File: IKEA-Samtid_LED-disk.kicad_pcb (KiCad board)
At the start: 2 copper layers, 40.5 x 40.5 mm, 0 parts

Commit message: Stuff.
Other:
- board size 40.5 x 40.5 mm -> 100 x 100 mm
- board text added: "align with spoke"
- board text added: "bottom keepout"
- board text added: "top keepout"
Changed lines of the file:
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@@
-(kicad_pcb (version 3) (host pcbnew "(2014-06-29 BZR 4957)-product")
+(kicad_pcb (version 4) (host pcbnew "(2014-07-07 BZR 4985)-product")
   (general
     (links 0)
     (no_connects 0)
-    (area 117.649999 62.649999 182.350001 127.350001)
+    (area 99.899999 44.899999 204.312359 145.100001)
     (thickness 1.6002)
-    (drawings 2)
+    (drawings 13)
     (tracks 0)
     (zones 0)
@@
   )
   (layers
-    (15 Front signal)
-    (0 Back signal)
-    (18 B.Paste user)
-    (19 F.Paste user)
-    (20 B.SilkS user)
-    (21 F.SilkS user)
-    (22 B.Mask user)
-    (23 F.Mask user)
-    (26 Eco1.User user)
-    (28 Edge.Cuts user)
+    (0 Front signal)
+    (31 Back signal)
+    (34 B.Paste user)
+    (35 F.Paste user)
+    (36 B.SilkS user)
+    (37 F.SilkS user)
+    (38 B.Mask user)
+    (39 F.Mask user)
+    (42 Eco1.User user)
+    (44 Edge.Cuts user)
   )
   (setup
@@
     (visible_elements 7FFFFF7F)
     (pcbplotparams
-      (layerselection 352092161)
+      (layerselection 0x014fc_80000001)
       (usegerberextensions true)
+      (gerberprecision 5)
       (excludeedgelayer true)
-      (linewidth 0.150000)
+      (linewidth 0.200000)
       (plotframeref false)
       (viasonmask false)
@@
     (uvia_drill 0.127)
   )
-  (gr_circle (center 150 95) (end 182.25 95) (layer Eco1.User) (width 0.2))
+  (gr_arc (start 150 95) (end 123.25 106.25) (angle 99.41721335) (layer F.SilkS) (width 0.2))
+  (gr_arc (start 150 95) (end 172.75 113) (angle 104.2890517) (layer F.SilkS) (width 0.2))
+  (gr_arc (start 150 95) (end 156.75 66.75) (angle 99.18167573) (layer F.SilkS) (width 0.2))
+  (gr_circle (center 150 95) (end 200 95) (layer Edge.Cuts) (width 0.2))
+  (gr_circle (center 150 68.75) (end 152.25 68.75) (layer Edge.Cuts) (width 0.2))
+  (gr_line (start 150 73) (end 150 64.5) (angle 90) (layer F.SilkS) (width 2))
+  (gr_text "align with \n\n\nspoke" (at 149.75 68.249999 90) (layer F.SilkS)
+    (effects (font (size 1.5 1.5) (thickness 0.3)))
+  )
+  (gr_text "top keepout" (at 176.499998 94.75 90) (layer F.SilkS)
+    (effects (font (size 1 1) (thickness 0.2)))
+  )
+  (gr_text "bottom keepout" (at 180.000002 94.750002 90) (layer B.SilkS)
+    (effects (font (size 1 1) (thickness 0.2)))
+  )
+  (gr_line (start 131 106) (end 123.5 110.25) (layer F.SilkS) (width 2))
+  (gr_line (start 169 106) (end 176.5 110.25) (layer F.SilkS) (width 2))
+  (gr_circle (center 150 95) (end 182.25 95) (layer B.SilkS) (width 0.2))
   (gr_circle (center 150 95) (end 170.25 95) (layer Edge.Cuts) (width 0.2))
 )

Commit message: More stuff.
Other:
- net class Default: clearance 0.2032 -> 0.254; trace_width 0.2032 -> 0.254; via_dia 0.635 -> 0.889; via_drill 0.3302 -> 0.635
- rule trace_clearance: 0.2032 -> 0.254
- rule trace_min: 0.2032 -> 0.254
- rule via_min_drill: 0.3302 -> 0.508
- rule via_min_size: 0.635 -> 0.889
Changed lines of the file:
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@@
-(kicad_pcb (version 4) (host pcbnew "(2014-07-07 BZR 4985)-product")
+(kicad_pcb (version 3) (host pcbnew "(2014-06-29 BZR 4957)-product")
   (general
     (links 0)
     (no_connects 0)
-    (area 99.899999 44.899999 204.312359 145.100001)
-    (thickness 1.6002)
+    (area 99.899999 44.899999 200.100001 145.100001)
+    (thickness 1.6)
     (drawings 13)
     (tracks 0)
@@
   )
   (layers
-    (0 Front signal)
-    (31 Back signal)
-    (34 B.Paste user)
-    (35 F.Paste user)
-    (36 B.SilkS user)
-    (37 F.SilkS user)
-    (38 B.Mask user)
-    (39 F.Mask user)
-    (42 Eco1.User user)
-    (44 Edge.Cuts user)
+    (15 F.Cu signal)
+    (0 B.Cu signal)
+    (18 B.Paste user)
+    (19 F.Paste user)
+    (20 B.SilkS user)
+    (21 F.SilkS user)
+    (22 B.Mask user)
+    (23 F.Mask user)
+    (26 Eco1.User user)
+    (28 Edge.Cuts user)
   )
   (setup
-    (last_trace_width 0.2032)
-    (user_trace_width 0.2032)
-    (user_trace_width 0.3048)
-    (user_trace_width 0.4064)
-    (user_trace_width 0.508)
-    (user_trace_width 0.762)
-    (user_trace_width 1.016)
-    (user_trace_width 1.27)
-    (trace_clearance 0.2032)
-    (zone_clearance 0.25)
+    (last_trace_width 0.254)
+    (trace_clearance 0.254)
+    (zone_clearance 0.508)
     (zone_45_only no)
-    (trace_min 0.2032)
+    (trace_min 0.254)
     (segment_width 0.2)
     (edge_width 0.2)
-    (via_size 0.635)
-    (via_drill 0.3302)
-    (via_min_size 0.635)
-    (via_min_drill 0.3302)
+    (via_size 0.889)
+    (via_drill 0.635)
+    (via_min_size 0.889)
+    (via_min_drill 0.508)
     (uvia_size 0.508)
     (uvia_drill 0.127)
@@
     (mod_text_size 1 1)
     (mod_text_width 0.2)
-    (pad_size 1.651 1.65)
-    (pad_drill 0)
+    (pad_size 1.8 3.4)
+    (pad_drill 0.6)
     (pad_to_mask_clearance 0)
     (aux_axis_origin 0 0)
-    (visible_elements 7FFFFF7F)
+    (visible_elements FFFFFF7F)
     (pcbplotparams
-      (layerselection 0x014fc_80000001)
+      (layerselection 352092161)
       (usegerberextensions true)
-      (gerberprecision 5)
       (excludeedgelayer true)
-      (linewidth 0.200000)
+      (linewidth 0.100000)
       (plotframeref false)
       (viasonmask false)
@@
       (hpglpenspeed 20)
       (hpglpendiameter 15)
-      (hpglpenoverlay 0)
+      (hpglpenoverlay 2)
       (psnegative false)
       (psa4output false)
@@
   (net 0 "")
   (net_class Default "This is the default net class."
-    (clearance 0.2032)
-    (trace_width 0.2032)
-    (via_dia 0.635)
-    (via_drill 0.3302)
+    (clearance 0.254)
+    (trace_width 0.254)
+    (via_dia 0.889)
+    (via_drill 0.635)
     (uvia_dia 0.508)
     (uvia_drill 0.127)

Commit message: Trying to be creative.
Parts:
- added LED?: VAL**, my_parts:MADW__PLCC4-5050, F.Cu at (150.2, 54.5)
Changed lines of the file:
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@@
     (tracks 0)
     (zones 0)
-    (modules 0)
+    (modules 1)
     (nets 1)
   )
@@
     (22 B.Mask user)
     (23 F.Mask user)
+    (25 Cmts.User user)
     (26 Eco1.User user)
     (28 Edge.Cuts user)
@@
       (plotinvisibletext false)
       (padsonsilk false)
-      (subtractmaskfromsilk true)
+      (subtractmaskfromsilk false)
       (outputformat 1)
       (mirror false)
@@
     (uvia_drill 0.127)
   )
+  (module my_parts:MADW__PLCC4-5050 (layer F.Cu)
+    (at 150.25 54.5)
+    (fp_text reference LED? (at 0 -4.75) (layer F.SilkS)
+      (effects (font (size 1 1) (thickness 0.2)))
+    )
+    (fp_text value VAL** (at 0 4.85) (layer F.SilkS) hide
+      (effects (font (size 1 1) (thickness 0.2)))
+    )
+    (fp_line (start 1.65 -1) (end 1.2 -0.25) (layer F.SilkS) (width 0.2032))
+    (fp_line (start 1.2 -0.25) (end 2.1 -0.25) (layer F.SilkS) (width 0.2032))
+    (fp_line (start 2.1 -0.25) (end 1.65 -1) (layer F.SilkS) (width 0.2032))
+    (fp_line (start -2.5 -1) (end -2.5 1) (layer F.SilkS) (width 0.2032))
+    (fp_line (start -0.5 2.5) (end 0.5 2.5) (layer F.SilkS) (width 0.2032))
+    (fp_line (start 2.5 -1) (end 2.5 1) (layer F.SilkS) (width 0.2032))
+    (fp_line (start -0.5 -2.5) (end 0.5 -2.5) (layer F.SilkS) (width 0.2032))
+    (fp_line (start 2.1 2.5) (end 2.5 2.5) (layer Dwgs.User) (width 0.2032))
+    (fp_line (start -1.2 2.5) (end 1.2 2.5) (layer Dwgs.User) (width 0.2032))
+    (fp_line (start -2.5 2.5) (end -2.1 2.5) (layer Dwgs.User) (width 0.2032))
+    (fp_line (start 2.1 -2.5) (end 2.5 -2.5) (layer Dwgs.User) (width 0.2032))
+    (fp_line (start -1.2 -2.5) (end 1.2 -2.5) (layer Dwgs.User) (width 0.2032))
+    (fp_line (start -2.5 -2.5) (end -2.1 -2.5) (layer Dwgs.User) (width 0.2032))
+    (fp_line (start -2.1 -2.7) (end -1.2 -2.7) (layer Dwgs.User) (width 0.2032))
+    (fp_line (start -1.2 -2.7) (end -1.2 -1.8) (layer Dwgs.User) (width 0.2032))
+    (fp_line (start -1.2 -1.8) (end -2.1 -1.8) (layer Dwgs.User) (width 0.2032))
+    (fp_line (start -2.1 -1.8) (end -2.1 -2.7) (layer Dwgs.User) (width 0.2032))
+    (fp_line (start 2.1 -2.7) (end 1.2 -2.7) (layer Dwgs.User) (width 0.2032))
+    (fp_line (start 1.2 -2.7) (end 1.2 -1.8) (layer Dwgs.User) (width 0.2032))
+    (fp_line (start 1.2 -1.8) (end 2.1 -1.8) (layer Dwgs.User) (width 0.2032))
+    (fp_line (start 2.1 -1.8) (end 2.1 -2.7) (layer Dwgs.User) (width 0.2032))
+    (fp_line (start -3 3.85) (end -3 -3.85) (layer F.SilkS) (width 0.2))
+    (fp_line (start 3 3.85) (end -3 3.85) (layer F.SilkS) (width 0.2))
+    (fp_line (start -3 -3.85) (end 3 -3.85) (layer F.SilkS) (width 0.2))
+    (fp_line (start 3 -3.85) (end 3 3.85) (layer F.SilkS) (width 0.2))
+    (fp_line (start -2.1 2.7) (end -2.1 1.8) (layer Dwgs.User) (width 0.2))
+    (fp_line (start -2.1 1.8) (end -1.2 1.8) (layer Dwgs.User) (width 0.2))
+    (fp_line (start -1.2 1.8) (end -1.2 2.7) (layer Dwgs.User) (width 0.2))
+    (fp_line (start -1.2 2.7) (end -2.1 2.7) (layer Dwgs.User) (width 0.2))
+    (fp_line (start 1.2 2.7) (end 1.2 1.8) (layer Dwgs.User) (width 0.2))
+    (fp_line (start 1.2 1.8) (end 2.1 1.8) (layer Dwgs.User) (width 0.2))
+    (fp_line (start 2.1 1.8) (end 2.1 2.7) (layer Dwgs.User) (width 0.2))
+    (fp_line (start 2.1 2.7) (end 1.2 2.7) (layer Dwgs.User) (width 0.2))
+    (fp_line (start 2.5 -2.5) (end 2.5 2.5) (layer Dwgs.User) (width 0.2))
+    (fp_line (start -2.49936 2.49936) (end -2.49936 -2.49936) (layer Dwgs.User) (width 0.2))
+    (pad 1 smd rect (at 1.65 -2.4) (size 1.4 1.8) (layers F.Cu F.Paste F.Mask))
+    (pad 2 smd rect (at -1.65 -2.4) (size 1.4 1.8) (layers F.Cu F.Paste F.Mask))
+    (pad 3 smd rect (at -1.65 2.4) (size 1.4 1.8) (layers F.Cu F.Paste F.Mask))
+    (pad 4 smd rect (at 1.65 2.4) (size 1.4 1.8) (layers F.Cu F.Paste F.Mask))
+  )
   (gr_arc (start 150 95) (end 123.25 106.25) (angle 99.41721335) (layer F.SilkS) (width 0.2))
   (gr_arc (start 150 95) (end 172.75 113) (angle 104.2890517) (layer F.SilkS) (width 0.2))
@@
     (effects (font (size 1.5 1.5) (thickness 0.3)))
   )
-  (gr_text "top keepout" (at 176.499998 94.75 90) (layer F.SilkS)
+  (gr_text "top keepout" (at 176.499998 94.75 90) (layer Cmts.User)
     (effects (font (size 1 1) (thickness 0.2)))
   )
-  (gr_text "bottom keepout" (at 180.000002 94.750002 90) (layer B.SilkS)
+  (gr_text "bottom keepout" (at 180.000002 94.750002 90) (layer Cmts.User)
     (effects (font (size 1 1) (thickness 0.2)))
   )

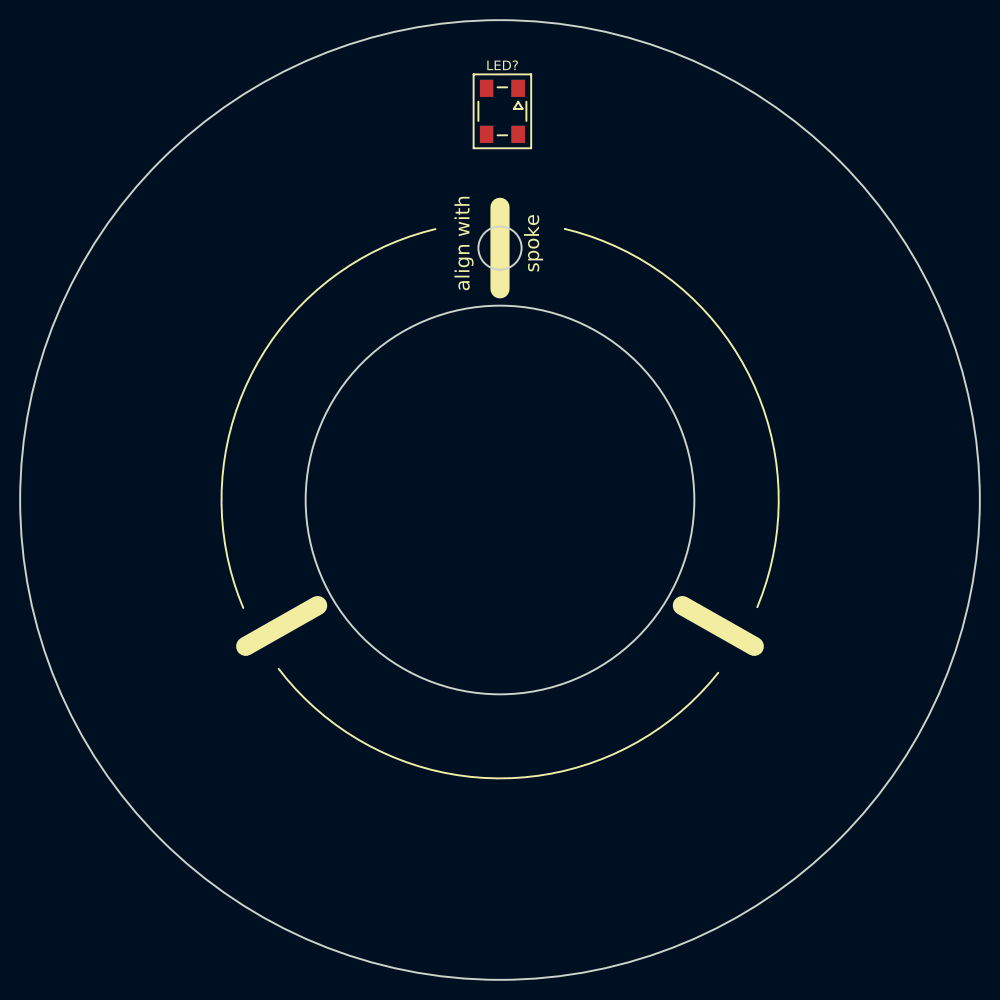
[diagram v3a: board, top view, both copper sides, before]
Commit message: Adding WS2812B footprints for testing board real-estate.
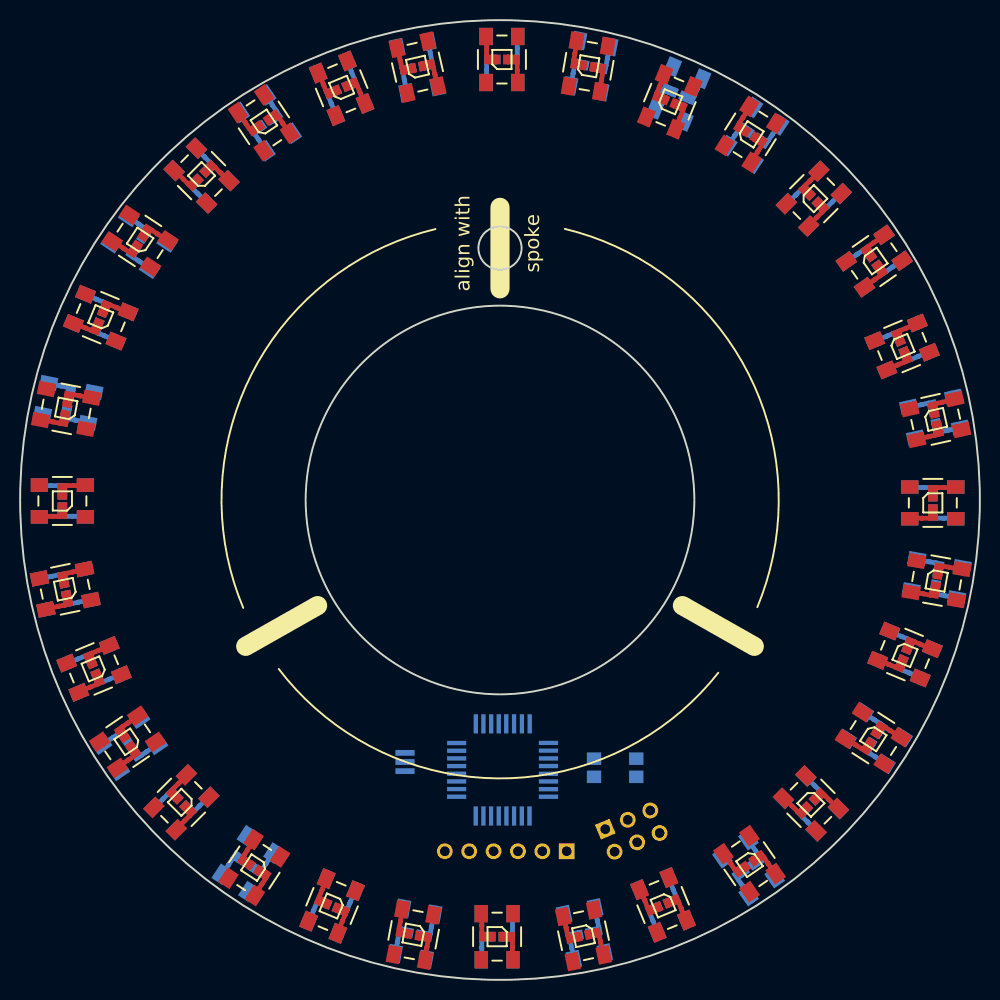
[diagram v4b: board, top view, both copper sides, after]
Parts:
- added C?: VAL**, my_parts:MADW__C0805, B.Cu at (159.8, 122.9)
- added C?: VAL**, my_parts:MADW__C0805, B.Cu at (164.2, 122.9)
- added IC?: VAL**, my_parts:MADW__TQFP_32_7x7, B.Cu at (150.3, 123.1)
- added LED?: VAL**, WS2812B:WS2812B_data-bridgeable, B.Cu at (118.9, 61.2)
- added LED?: VAL**, WS2812B:WS2812B_data-bridgeable, F.Cu at (116.8, 126.5)
- added LED?: VAL**, WS2812B:WS2812B_data-bridgeable, F.Cu at (182.4, 126.6)
- added LED?: VAL**, WS2812B:WS2812B_data-bridgeable, F.Cu at (182.7, 63.6)
- added LED?: VAL**, WS2812B:WS2812B_data-bridgeable, F.Cu at (118.9, 61.2)
- added LED?: VAL**, WS2812B:WS2812B_data-bridgeable, F.Cu at (104.4, 95.1)
- added LED?: VAL**, WS2812B:WS2812B_data-bridgeable, F.Cu at (149.7, 140.5)
- added LED?: VAL**, WS2812B:WS2812B_data-bridgeable, F.Cu at (195.1, 95.3)
- added LED?: VAL**, WS2812B:WS2812B_data-bridgeable, B.Cu at (150.2, 49.1)
- added LED?: VAL**, WS2812B:WS2812B_data-bridgeable, B.Cu at (133.5, 52.1)
- added LED?: VAL**, WS2812B:WS2812B_data-bridgeable, F.Cu at (107.7, 112.6)
- added LED?: VAL**, WS2812B:WS2812B_data-bridgeable, B.Cu at (108.4, 76.0)
- added LED?: VAL**, WS2812B:WS2812B_data-bridgeable, B.Cu at (182.7, 63.6)
- added LED?: VAL**, WS2812B:WS2812B_data-bridgeable, B.Cu at (168.6, 52.7)
- added LED?: VAL**, WS2812B:WS2812B_data-bridgeable, B.Cu at (104.4, 95.1)
- added LED?: VAL**, WS2812B:WS2812B_data-bridgeable, B.Cu at (107.7, 112.6)
- added LED?: VAL**, WS2812B:WS2812B_data-bridgeable, B.Cu at (167.0, 137.2)
- added LED?: VAL**, WS2812B:WS2812B_data-bridgeable, B.Cu at (149.7, 140.5)
- added LED?: VAL**, WS2812B:WS2812B_data-bridgeable, B.Cu at (192.2, 111.1)
- added LED?: VAL**, WS2812B:WS2812B_data-bridgeable, B.Cu at (182.4, 126.6)
- added LED?: VAL**, WS2812B:WS2812B_data-bridgeable, B.Cu at (195.1, 95.3)
- added LED?: VAL**, WS2812B:WS2812B_data-bridgeable, F.Cu at (132.5, 137.3)
- added LED?: VAL**, WS2812B:WS2812B_data-bridgeable, B.Cu at (191.9, 79.0)
- added LED?: VAL**, WS2812B:WS2812B_data-bridgeable, B.Cu at (116.8, 126.5)
- added LED?: VAL**, WS2812B:WS2812B_data-bridgeable, B.Cu at (132.5, 137.3)
- added LED?: VAL**, WS2812B:WS2812B_data-bridgeable, F.Cu at (141.4, 49.9)
- added LED?: VAL**, WS2812B:WS2812B_data-bridgeable, F.Cu at (125.4, 55.7)
- added LED?: VAL**, WS2812B:WS2812B_data-bridgeable, F.Cu at (112.5, 68.0)
- added LED?: VAL**, WS2812B:WS2812B_data-bridgeable, F.Cu at (104.8, 85.5)
- added LED?: VAL**, WS2812B:WS2812B_data-bridgeable, F.Cu at (104.7, 104.3)
- added LED?: VAL**, WS2812B:WS2812B_data-bridgeable, F.Cu at (111.2, 120.2)
- added LED?: VAL**, WS2812B:WS2812B_data-bridgeable, F.Cu at (124.4, 133.3)
- added LED?: VAL**, WS2812B:WS2812B_data-bridgeable, F.Cu at (167.0, 137.2)
- added LED?: VAL**, WS2812B:WS2812B_data-bridgeable, F.Cu at (141.0, 140.3)
- added LED?: VAL**, WS2812B:WS2812B_data-bridgeable, F.Cu at (158.7, 140.4)
- added LED?: VAL**, WS2812B:WS2812B_data-bridgeable, F.Cu at (176.0, 132.9)
- added LED?: VAL**, WS2812B:WS2812B_data-bridgeable, F.Cu at (188.9, 119.8)
- added LED?: VAL**, WS2812B:WS2812B_data-bridgeable, F.Cu at (195.5, 103.4)
- added LED?: VAL**, WS2812B:WS2812B_data-bridgeable, F.Cu at (195.4, 86.6)
- added LED?: VAL**, WS2812B:WS2812B_data-bridgeable, F.Cu at (189.0, 70.1)
- added LED?: VAL**, WS2812B:WS2812B_data-bridgeable, F.Cu at (176.1, 56.9)
- added LED?: VAL**, WS2812B:WS2812B_data-bridgeable, F.Cu at (159.2, 49.8)
- added LED?: VAL**, WS2812B:WS2812B_data-bridgeable, B.Cu at (141.4, 49.9)
- added LED?: VAL**, WS2812B:WS2812B_data-bridgeable, F.Cu at (192.2, 111.1)
- added LED?: VAL**, WS2812B:WS2812B_data-bridgeable, B.Cu at (125.6, 55.7)
- added LED?: VAL**, WS2812B:WS2812B_data-bridgeable, B.Cu at (112.4, 68.2)
- added LED?: VAL**, WS2812B:WS2812B_data-bridgeable, B.Cu at (105.0, 84.9)
- added LED?: VAL**, WS2812B:WS2812B_data-bridgeable, B.Cu at (104.7, 104.3)
- added LED?: VAL**, WS2812B:WS2812B_data-bridgeable, B.Cu at (111.4, 120.5)
- added LED?: VAL**, WS2812B:WS2812B_data-bridgeable, B.Cu at (123.7, 132.9)
- added LED?: VAL**, WS2812B:WS2812B_data-bridgeable, B.Cu at (141.1, 140.2)
- added LED?: VAL**, WS2812B:WS2812B_data-bridgeable, B.Cu at (158.8, 140.2)
- added LED?: VAL**, WS2812B:WS2812B_data-bridgeable, B.Cu at (175.9, 133.3)
- added LED?: VAL**, WS2812B:WS2812B_data-bridgeable, B.Cu at (189.0, 119.8)
- added LED?: VAL**, WS2812B:WS2812B_data-bridgeable, F.Cu at (191.9, 79.0)
- added LED?: VAL**, WS2812B:WS2812B_data-bridgeable, B.Cu at (195.5, 103.2)
- added LED?: VAL**, WS2812B:WS2812B_data-bridgeable, B.Cu at (195.3, 86.4)
- added LED?: VAL**, WS2812B:WS2812B_data-bridgeable, B.Cu at (189.0, 70.1)
- added LED?: VAL**, WS2812B:WS2812B_data-bridgeable, B.Cu at (176.4, 57.0)
- added LED?: VAL**, WS2812B:WS2812B_data-bridgeable, B.Cu at (159.4, 49.8)
- added LED?: VAL**, WS2812B:WS2812B_data-bridgeable, F.Cu at (167.7, 53.5)
- added LED?: VAL**, WS2812B:WS2812B_data-bridgeable, F.Cu at (133.5, 52.1)
- added LED?: VAL**, WS2812B:WS2812B_data-bridgeable, F.Cu at (108.4, 76.0)
- added P?: VAL**, my_parts:MADW__SIL-6, B.Cu at (150.6, 131.6)
- added P?: VAL**, my_parts:MADW__PIN_ARRAY_3x2_2.54mm, B.Cu at (163.8, 129.5)
- added X?: VAL**, my_parts:MADW__murata-resonator__CSTCE16M0V53-R0, B.Cu at (140.1, 122.3)
- LED?: footprint my_parts:MADW__PLCC4-5050 -> WS2812B:WS2812B_data-bridgeable
- moved LED? 5.40 mm to (150.2, 49.1)
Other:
- board text added: "fix the angles!"
